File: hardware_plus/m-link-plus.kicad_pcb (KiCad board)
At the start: 4 copper layers, 24 x 30 mm, 30 parts, among them J3 SIG, J4 PROGRAM, J5 I2C, SW1 RESTORE SETTINGS, U1 AP1117-33, U2 DRV8837C, U3 DRV8837C, U4 ESP-12F, U5 PCA9685PW, U6 DRV8837C

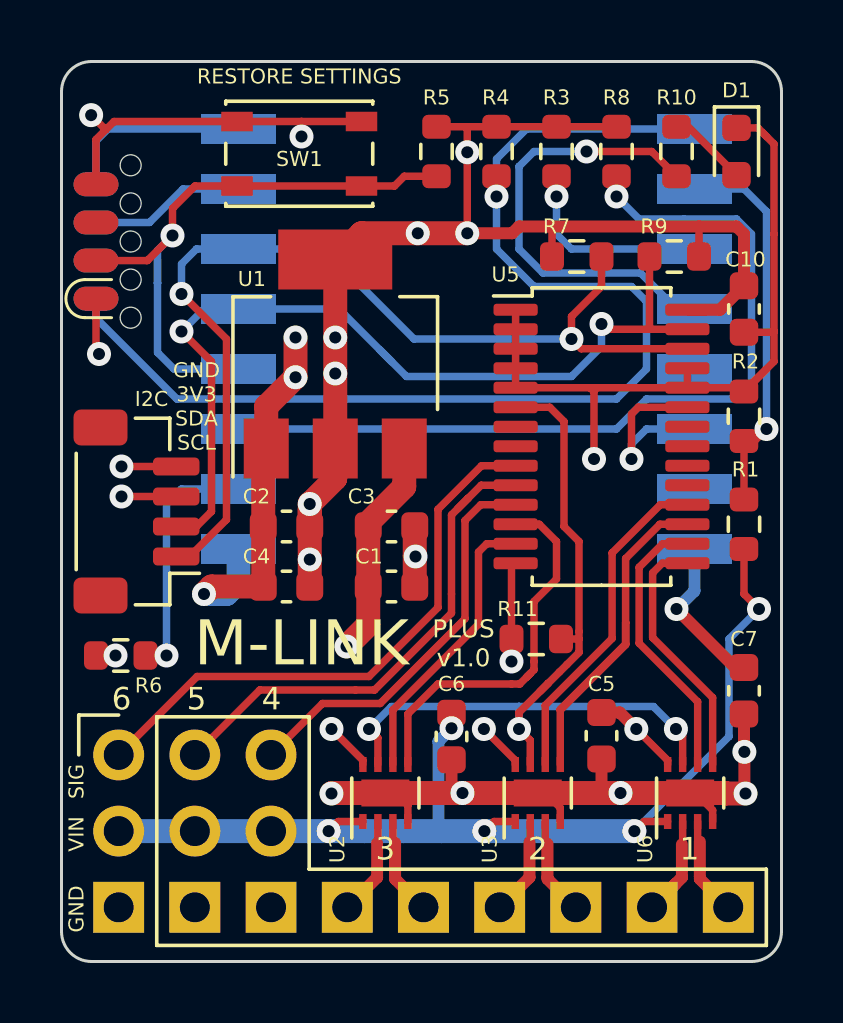
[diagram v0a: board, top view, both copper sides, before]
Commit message: Rework M-Link Plus by swapping the PCA9865 and the regulator.
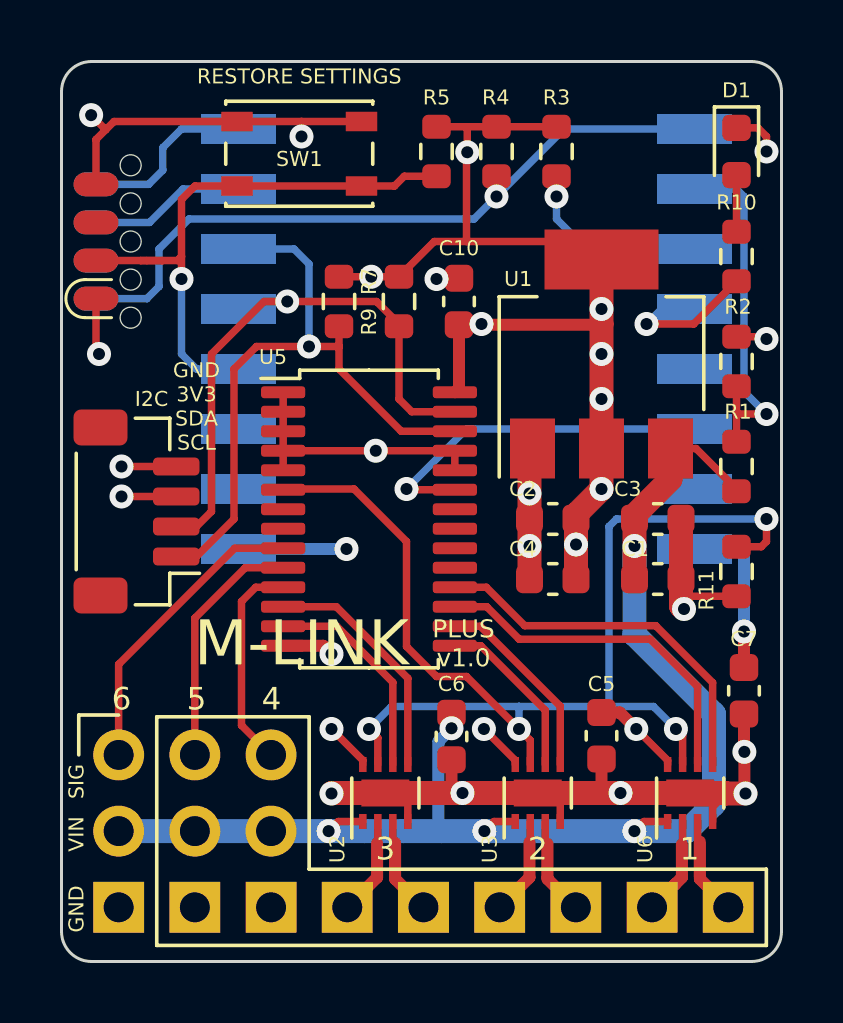
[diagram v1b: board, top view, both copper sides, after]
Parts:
- removed R6, R8: 10k, Resistor_SMD:R_0603_1608Metric
- moved C10 9.50 mm to (92.2, 77.0), turned to 90 degrees
- moved R9 9.30 mm to (90.2, 77.0), turned to 90 degrees
- moved C1 8.88 mm to (98.9, 86.2)
- moved C2 8.88 mm to (95.4, 84.2)
- moved C3 8.88 mm to (98.9, 84.2)
- moved C4 8.88 mm to (95.4, 86.2)
- moved U1 8.88 mm to (97.0, 78.8)
- moved U5 8.22 mm to (89.2, 84.2)
- moved R7 8.07 mm to (88.2, 77.0), turned to 90 degrees
- moved R11 7.04 mm to (101.5, 86.0), turned to 90 degrees
- moved R10 4.03 mm to (101.5, 75.5)
- moved R1 1.94 mm to (101.5, 82.5)
- moved R2 1.84 mm to (101.5, 79.0)
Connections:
- U4 pad 16: /MTDI -> unconnected-(U4-Pad16)
- U4 pad 17: /OE -> unconnected-(U4-Pad17)
- U5 pad 15: /CH9 -> /CH6
- U5 pad 16: /CH8 -> /CH7
- U5 pad 17: /CH7 -> /CH8
- U5 pad 18: /CH6 -> /CH9
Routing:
- net /OE: track 28.4 -> 0.00 mm, vias 1 -> 0
- net GND: track 83.9 -> 68.3 mm, vias 15 -> 17
- net /RESET: track 39.2 -> 23.7 mm
- net /SLEEP: track 29.6 -> 41.9 mm, vias 3 -> 4
- net /SCL: track 32.9 -> 22.7 mm, vias 2 -> 1
- net /SDA: track 30.1 -> 20.2 mm, vias 2 -> 1
- net /LED1: track 15.2 -> 5.40 mm
- net /CH1: track 19.1 -> 10.1 mm
- net /CH2: track 16.8 -> 8.20 mm
- net /MTDI: track 8.36 -> 0.00 mm, vias 1 -> 0
- net /CH7: track 14.1 -> 6.56 mm
- net +5V: track 52.9 -> 45.4 mm, vias 6 -> 5
- net /CH3: track 13.5 -> 7.11 mm
- net /ENABLE: track 6.26 -> 12.1 mm
- net /CH6: track 11.1 -> 5.71 mm
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
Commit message: Add resistors back to GPIO2 and GPIO15.
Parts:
- added R6: 10k, Resistor_SMD:R_0603_1608Metric, F.Cu at (86.2, 77.0)
- added R8: 10k, Resistor_SMD:R_0603_1608Metric, F.Cu at (84.2, 77.0)
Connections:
- U4 pad 16: unconnected-(U4-Pad16) -> Net-(U4-Pad16)
- U4 pad 17: unconnected-(U4-Pad17) -> Net-(U4-Pad17)
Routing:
- net Net-(U4-Pad16): track 0.00 -> 9.71 mm, vias 0 -> 1
- net Net-(U4-Pad17): track 0.00 -> 6.55 mm, vias 0 -> 1
- net +3V3: track 51.6 -> 57.5 mm
- net GND: track 68.3 -> 71.6 mm, vias 17 -> 18
- net /SDA: track 20.2 -> 21.9 mm
- net /SCL: track 22.7 -> 24.4 mm
- net /DTR: track 19.7 -> 18.6 mm

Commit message: Plot M-Link Plus v1.0
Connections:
- net Net-(U4-Pad16) renamed /MTDI
- net Net-(U4-Pad17) renamed /ESP_LED
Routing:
- net GND: track 71.6 -> 76.0 mm
- net +5V: track 45.4 -> 44.3 mm
- net +3V3: track 57.5 -> 56.5 mm, vias 14 -> 13
- net /SLEEP: track 41.9 -> 41.4 mm
- net /CH9: track 12.6 -> 12.1 mm
- net /CH8: track 11.8 -> 11.3 mm
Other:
- board text added: "3V3"
- board text added: "DTR"
- board text added: "RST"
- board text added: "RX"
- board text added: "SCL"
- board text added: "SDA"
- board text added: "TX"
- board text removed: "GND 3V3 SDA SCL"

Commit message: Improve ground plane.
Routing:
- net GND: track 76.0 -> 88.7 mm
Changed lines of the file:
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@@
   (via (at 101.762299 92.012299) (size 0.8) (drill 0.4) (layers "F.Cu" "B.Cu") (net 1))
   (via (at 102.5 78.25) (size 0.8) (drill 0.4) (layers "F.Cu" "B.Cu") (net 1))
-  (segment (start 83.445 97.194) (end 84.794 97.194) (width 0.25) (layer "In1.Cu") (net 1))
+  (segment (start 83.445 97.194) (end 84.694 97.194) (width 0.25) (layer "In1.Cu") (net 1))
+  (segment (start 84.695 97.193) (end 84.695 93.695) (width 0.4) (layer "In1.Cu") (net 1))
+  (segment (start 84.694 97.194) (end 84.695 97.193) (width 0.4) (layer "In1.Cu") (net 1))
+  (segment (start 84.694 97.194) (end 84.794 97.194) (width 0.25) (layer "In1.Cu") (net 1))
+  (segment (start 84.695 93.695) (end 84.5 93.5) (width 0.4) (layer "In1.Cu") (net 1))
+  (segment (start 80.905 97.194) (end 85.985 97.194) (width 0.4) (layer "In1.Cu") (net 1))
+  (segment (start 82.194 97.194) (end 82.194 93.694) (width 0.4) (layer "In1.Cu") (net 1))
   (segment (start 82.194 97.194) (end 83.445 97.194) (width 0.25) (layer "In1.Cu") (net 1))
+  (segment (start 82.194 93.694) (end 82 93.5) (width 0.4) (layer "In1.Cu") (net 1))
   (segment (start 84.794 97.194) (end 85.985 97.194) (width 0.25) (layer "In1.Cu") (net 1))
   (segment (start 80.905 97.194) (end 82.194 97.194) (width 0.25) (layer "In1.Cu") (net 1))
